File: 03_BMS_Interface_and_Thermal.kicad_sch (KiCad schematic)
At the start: 43 parts, among them J1 HDR-1X17_2.54mm [C22549], J2 S16B-XH-A [C157933]

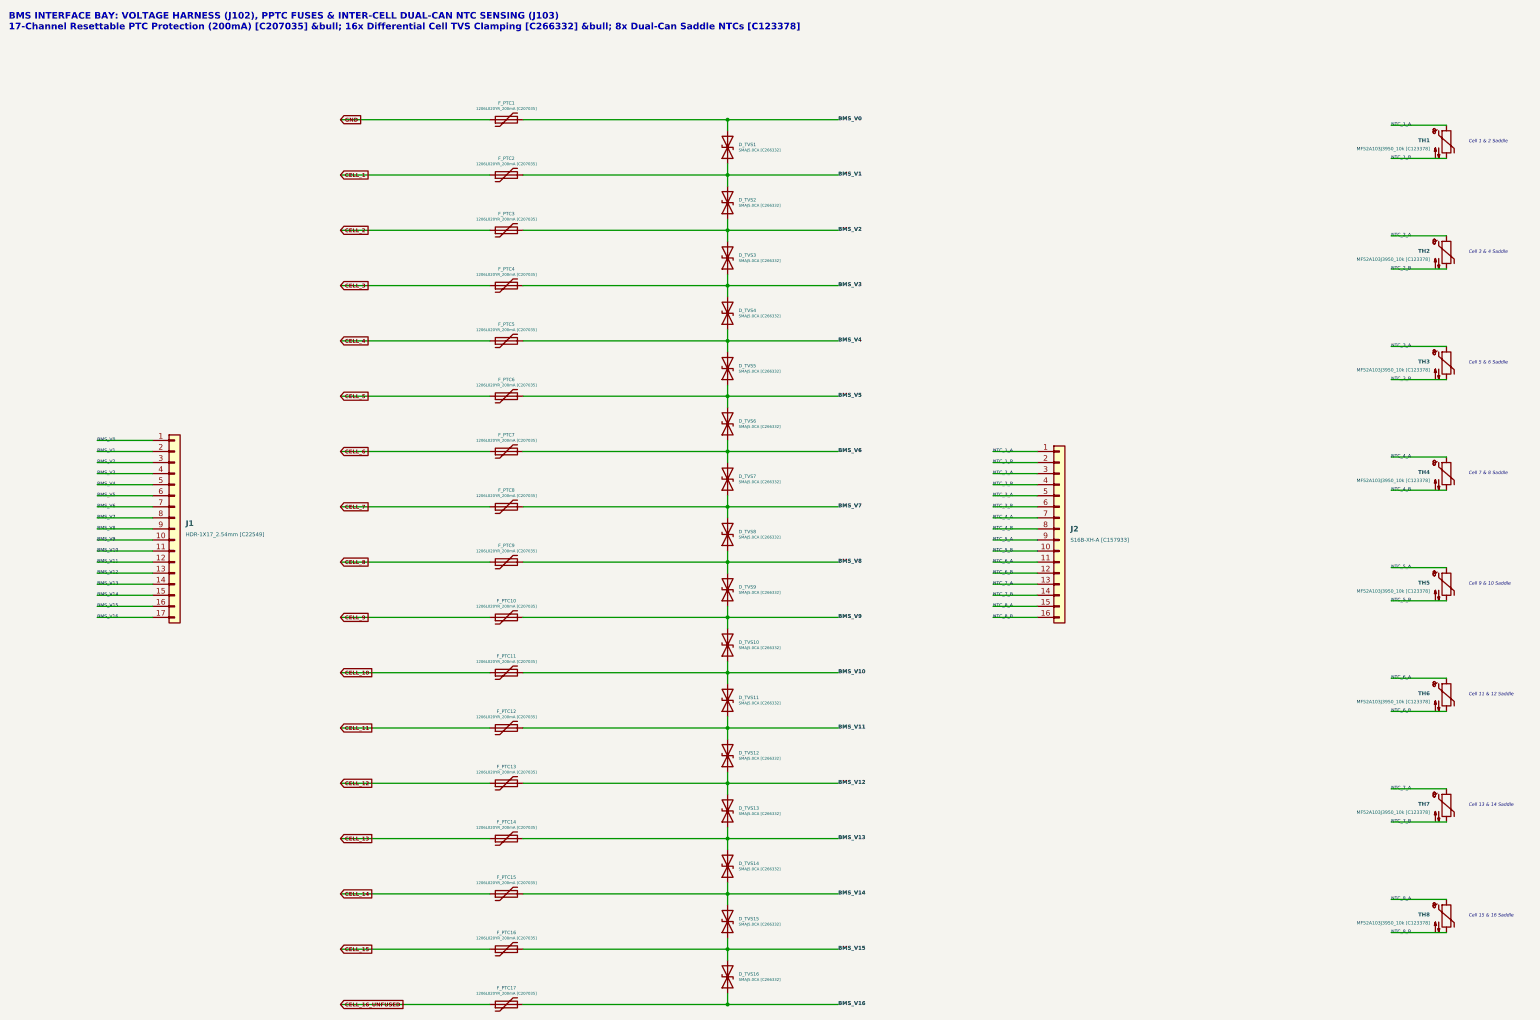
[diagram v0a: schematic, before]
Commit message: Convert pack to 14S with 7 NTC sensors, JST XH harness connectors, all-JLC BOM
- Schematic regenerated: 14 cells, 15-wire BMS sense on JST XH B15B-XH-A,
  7x 10k B3950 NTC saddles on JST XH B14B-XH-A, per-cell test loops and
  reverse-insertion indicator, power path with 5x20 fuse and M4 lugs.
- Fixes: HV zener was reversed, 4.7k/1206 HV LED resistor dissipated 0.68W
  (now 22k), 24V PPTCs on sense taps replaced with 60V MF-MSMF010-2,
  fuse-blown LED polarity corrected.
- Banana jacks (not stocked at LCSC) replaced by Keystone 5000/5001 loops.
- PCB re-laid out on the A4 (297x210) 4-layer outline: 8+6 cell columns,
  zones for cell links, sense routed on In1, NTC pairs on In2.
- ERC 0, DRC 0 (all severities), 0 unconnected, 0 schematic parity issues.
- Added Gerbers/drill zip, JLCPCB BOM + CPL, schematic PDF, renders, and the
  generator scripts in tools/.

Co-Authored-By: Claude Opus 5.5 <noreply@anthropic.com>
Claude-Session: https://claude.ai/code/session_01SDBUxKR8a94h5ECbt5NLbF
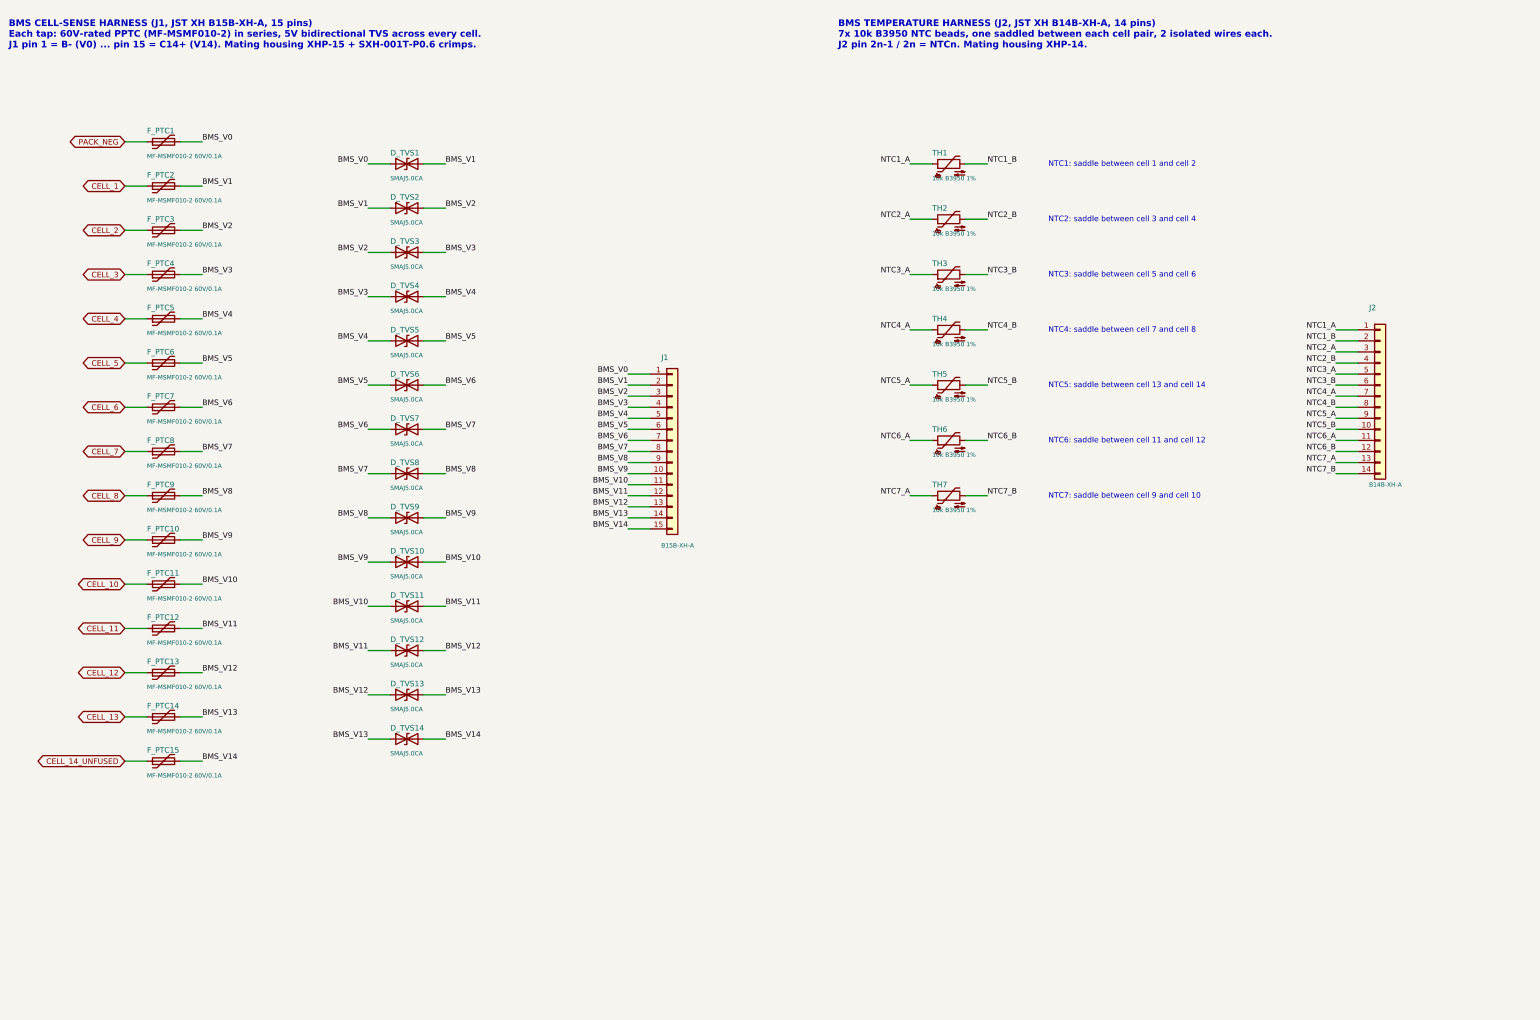
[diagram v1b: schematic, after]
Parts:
- removed D_TVS15, D_TVS16: SMAJ5.0CA [C266332], Diode_SMD:D_SMA, symbol Device:D_TVS
- removed F_PTC16, F_PTC17: 1206L020YR_200mA [C207035], Resistor_SMD:R_1206_3216Metric, symbol Device:Polyfuse
- removed J1: HDR-1X17_2.54mm [C22549], Connector_PinHeader_2.54mm:PinHeader_1x17_P2.54mm_Horizontal, symbol Connector_Generic:Conn_01x17
- removed J2: S16B-XH-A [C157933], Connector_JST:JST_XH_S16B-XH-A_1x16_P2.50mm_Horizontal, symbol Connector_Generic:Conn_01x16
- removed TH8: MF52A103J3950_10k [C123378], Resistor_THT:R_Axial_DIN0204_L3.6mm_D1.6mm_P2.54mm_Vertical, symbol Device:Thermistor_NTC
- added J1: B15B-XH-A, Connector_JST:JST_XH_B15B-XH-A_1x15_P2.50mm_Vertical, symbol Connector_Generic:Conn_01x15
- added J2: B14B-XH-A, Connector_JST:JST_XH_B14B-XH-A_1x14_P2.50mm_Vertical, symbol Connector_Generic:Conn_01x14
- D_TVS1, D_TVS10, D_TVS11, D_TVS12, D_TVS13, D_TVS14, D_TVS2, D_TVS3, D_TVS4, D_TVS5, D_TVS6, D_TVS7, D_TVS8, D_TVS9: value SMAJ5.0CA [C266332] -> SMAJ5.0CA; JLCPCB Part # C266332 -> (none); LCSC C266332 -> C5174731; Manufacturer (none) -> JSCJ
- F_PTC1, F_PTC10, F_PTC11, F_PTC12, F_PTC13, F_PTC14, F_PTC15, F_PTC2, F_PTC3, F_PTC4, F_PTC5, F_PTC6, F_PTC7, F_PTC8, F_PTC9: value 1206L020YR_200mA [C207035] -> MF-MSMF010-2 60V/0.1A; footprint Resistor_SMD:R_1206_3216Metric -> Fuse:Fuse_1812_4532Metric; JLCPCB Part # C207035 -> (none); LCSC C207035 -> C12430; MPN 1206L020YR -> MF-MSMF010-2; Manufacturer (none) -> BOURNS
- TH1, TH2, TH3, TH4, TH5, TH6, TH7: value MF52A103J3950_10k [C123378] -> 10k B3950 1%; JLCPCB Part # C123378 -> (none); LCSC C123378 -> C13879; MPN MF52A103J3950 -> MF52A103F3950; Manufacturer (none) -> Nanjing Shiheng
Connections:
- net BMS_V0: now also D_TVS1.1 (A1), J1.1 (Pin_1); no longer D_TVS1.2 (A2)
- net BMS_V1: now also D_TVS1.2 (A2), D_TVS2.1 (A1), J1.2 (Pin_2); no longer D_TVS1.1 (A1), D_TVS2.2 (A2)
- net BMS_V10: now also D_TVS10.2 (A2), D_TVS11.1 (A1), J1.11 (Pin_11); no longer D_TVS10.1 (A1), D_TVS11.2 (A2)
- net BMS_V11: now also D_TVS11.2 (A2), D_TVS12.1 (A1), J1.12 (Pin_12); no longer D_TVS11.1 (A1), D_TVS12.2 (A2)
- net BMS_V12: now also D_TVS12.2 (A2), D_TVS13.1 (A1), J1.13 (Pin_13); no longer D_TVS12.1 (A1), D_TVS13.2 (A2)
- net BMS_V13: now also D_TVS13.2 (A2), D_TVS14.1 (A1), J1.14 (Pin_14); no longer D_TVS13.1 (A1), D_TVS14.2 (A2)
- net BMS_V14: now also D_TVS14.2 (A2), J1.15 (Pin_15); no longer D_TVS14.1 (A1)
- net BMS_V2: now also D_TVS2.2 (A2), D_TVS3.1 (A1), J1.3 (Pin_3); no longer D_TVS2.1 (A1), D_TVS3.2 (A2)
- net BMS_V3: now also D_TVS3.2 (A2), D_TVS4.1 (A1), J1.4 (Pin_4); no longer D_TVS3.1 (A1), D_TVS4.2 (A2)
- net BMS_V4: now also D_TVS4.2 (A2), D_TVS5.1 (A1), J1.5 (Pin_5); no longer D_TVS4.1 (A1), D_TVS5.2 (A2)
- net BMS_V5: now also D_TVS5.2 (A2), D_TVS6.1 (A1), J1.6 (Pin_6); no longer D_TVS5.1 (A1), D_TVS6.2 (A2)
- net BMS_V6: now also D_TVS6.2 (A2), D_TVS7.1 (A1), J1.7 (Pin_7); no longer D_TVS6.1 (A1), D_TVS7.2 (A2)
- net BMS_V7: now also D_TVS7.2 (A2), D_TVS8.1 (A1), J1.8 (Pin_8); no longer D_TVS7.1 (A1), D_TVS8.2 (A2)
- net BMS_V8: now also D_TVS8.2 (A2), D_TVS9.1 (A1), J1.9 (Pin_9); no longer D_TVS8.1 (A1), D_TVS9.2 (A2)
- net BMS_V9: now also D_TVS10.1 (A1), D_TVS9.2 (A2), J1.10 (Pin_10); no longer D_TVS10.2 (A2), D_TVS9.1 (A1)
- net CELL_14 renamed CELL_14_UNFUSED
- net GND renamed PACK_NEG
- net NTC_1_A renamed NTC1_A
- net NTC1_A: now also J2.1 (Pin_1)
- net NTC_1_B renamed NTC1_B
- net NTC1_B: now also J2.2 (Pin_2)
- net NTC_2_A renamed NTC2_A
- net NTC2_A: now also J2.3 (Pin_3)
- net NTC_2_B renamed NTC2_B
- net NTC2_B: now also J2.4 (Pin_4)
- net NTC_3_A renamed NTC3_A
- net NTC3_A: now also J2.5 (Pin_5)
- net NTC_3_B renamed NTC3_B
- net NTC3_B: now also J2.6 (Pin_6)
- net NTC_4_A renamed NTC4_A
- net NTC4_A: now also J2.7 (Pin_7)
- net NTC_4_B renamed NTC4_B
- net NTC4_B: now also J2.8 (Pin_8)
- net NTC_5_A renamed NTC5_A
- net NTC5_A: now also J2.9 (Pin_9)
- net NTC_5_B renamed NTC5_B
- net NTC5_B: now also J2.10 (Pin_10)
- net NTC_6_A renamed NTC6_A
- net NTC6_A: now also J2.11 (Pin_11)
- net NTC_6_B renamed NTC6_B
- net NTC6_B: now also J2.12 (Pin_12)
- net NTC_7_A renamed NTC7_A
- net NTC7_A: now also J2.13 (Pin_13)
- net NTC_7_B renamed NTC7_B
- net NTC7_B: now also J2.14 (Pin_14)
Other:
- note added: "BMS CELL-SENSE HARNESS (J1, JST XH B15B-XH-A, 15 pins) Each tap: 60V-rated PPTC (MF-MSMF010-2) in series, 5V bidirectional TVS across every cell. J1 pin 1 = B- (V0) ... pin 15 = C14+ (V14). Mating housing XHP-15 + SXH-001T-P0.6 crimps."
- note added: "BMS TEMPERATURE HARNESS (J2, JST XH B14B-XH-A, 14 pins) 7x 10k B3950 NTC beads, one saddled between each cell pair, 2 isolated wires each. J2 pin 2n-1 / 2n = NTCn. Mating housing XHP-14."
- note added: "NTC1: saddle between cell 1 and cell 2"
- note added: "NTC2: saddle between cell 3 and cell 4"
- note added: "NTC3: saddle between cell 5 and cell 6"
- note added: "NTC4: saddle between cell 7 and cell 8"
- note added: "NTC5: saddle between cell 13 and cell 14"
- note added: "NTC6: saddle between cell 11 and cell 12"
- note added: "NTC7: saddle between cell 9 and cell 10"
- note removed: "BMS INTERFACE BAY: VOLTAGE HARNESS (J102), PPTC FUSES & INTER-CELL DUAL-CAN NTC SENSING (J103) 17-Channel Resettable PTC Protection (200mA) [C207035] &bull; 16x Differential Cell TVS Clamping [C266332] &bull; 8x Dual-Can Saddle NTCs [C123378]"
- note removed: "Cell 1 & 2 Saddle"
- note removed: "Cell 11 & 12 Saddle"
- note removed: "Cell 13 & 14 Saddle"
- note removed: "Cell 15 & 16 Saddle"
- note removed: "Cell 3 & 4 Saddle"
- note removed: "Cell 5 & 6 Saddle"
- note removed: "Cell 7 & 8 Saddle"
- note removed: "Cell 9 & 10 Saddle"
- company: Antigravity Battery Engineering -> Battery Pack Breakout - 14S / A4
- title: BMS INTERFACE BAY: VOLTAGE HARNESS, PPTCS & THERMAL MONITORING -> BMS INTERFACE: 15-WIRE CELL SENSE + 7x NTC

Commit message: Mirror the two cell columns (7+7) and move every external connector to the top edge
- Cells 1-7 down the left column, 8-14 up the right, identical row spacing;
  B- now lands at the top-left corner and cell 14+ at the top-right.
- Top edge, left to right: J2 NTC, B- lug, J1 balance (centred), PACK+ lug,
  5x20 fuse. Balance pin 1 = B- on the left, matching the cell order.
- PPTC/TVS sense block sits directly under J1; sense taps fan in on In1,
  NTC pairs run up to J2 on In2. NTCs renumbered along the series path.
- Pack TVS and HV indicator next to PACK+, PACK- return on a B.Cu strip.
- Mid-board M3 holes moved into the channel; wiring guide on silkscreen.
- ERC 0, DRC 0 (all severities), 0 unconnected, 0 parity issues.

Co-Authored-By: Claude Opus 5.5 <noreply@anthropic.com>
Claude-Session: https://claude.ai/code/session_01SDBUxKR8a94h5ECbt5NLbF
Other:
- note added: "NTC4: saddle between cell 6 and cell 7"
- note added: "NTC5: saddle between cell 9 and cell 10"
- note added: "NTC7: saddle between cell 13 and cell 14"
- note removed: "NTC4: saddle between cell 7 and cell 8"
- note removed: "NTC5: saddle between cell 13 and cell 14"
- note removed: "NTC7: saddle between cell 9 and cell 10"
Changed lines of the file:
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@@
 		)
 	)
-	(text "NTC4: saddle between cell 7 and cell 8"
+	(text "NTC4: saddle between cell 6 and cell 7"
 		(exclude_from_sim no)
 		(at 264.16 93.345 0)
@@
 		)
 	)
-	(text "NTC5: saddle between cell 13 and cell 14"
+	(text "NTC5: saddle between cell 9 and cell 10"
 		(exclude_from_sim no)
 		(at 264.16 106.045 0)
@@
 		)
 	)
-	(text "NTC7: saddle between cell 9 and cell 10"
+	(text "NTC7: saddle between cell 13 and cell 14"
 		(exclude_from_sim no)
 		(at 264.16 131.445 0)

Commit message: Senior-level layout rework: equal-resistance cell links, uniform pitch, sense spine
- Uniform 27.6 mm cell pitch (4.8 mm air gap around every cell).
- All 13 cell-to-cell links are identical copper straps (F.Cu + B.Cu); the
  cell 7->8 strap across the channel is widened to 16.15 mm so its
  resistance matches. 2-D field solve: 0.260 mOhm per link, 0.08 % spread
  (tools/acir.py, docs/acir_check.txt).
- Centre channel is now a sense spine: a 60 V PPTC at every node and one
  In1 bus into J1; per-cell TVS moved to SOD-323 (LKS05D3-B) directly under
  J1 so the whole BMS protection block sits on the top edge.
- Outer margins: per-cell test loops, reverse-cell LED, writable V/IR box.
- Top edge: B- lug, HV indicator + pack TVS, J1, J2, PACK+ lug, fuse.
- Shared geometry module (tools/geom.py) used by layout and ACIR check.
- ERC 0, DRC 0, 0 unconnected, 0 parity issues.

Co-Authored-By: Claude Opus 5.5 <noreply@anthropic.com>
Claude-Session: https://claude.ai/code/session_01SDBUxKR8a94h5ECbt5NLbF
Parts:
- D_TVS1, D_TVS10, D_TVS11, D_TVS12, D_TVS13, D_TVS14, D_TVS2, D_TVS3, D_TVS4, D_TVS5, D_TVS6, D_TVS7, D_TVS8, D_TVS9: value SMAJ5.0CA -> LKS05D3-B; footprint Diode_SMD:D_SMA -> Diode_SMD:D_SOD-323; LCSC C5174731 -> C2984829; MPN SMAJ5.0CA -> LKS05D3-B; Manufacturer JSCJ -> LANKE
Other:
- note added: "BMS CELL-SENSE HARNESS (J1, JST XH B15B-XH-A, 15 pins) Each tap: 60V PPTC (MF-MSMF010-2) next to its cell node, 5V bidir TVS (LKS05D3-B) across every cell at J1. J1 pin 1 = B- (V0) ... pin 15 = C14+ (V14). Mating housing XHP-15 + SXH-001T-P0.6 crimps."
- note added: "NTC5: saddle between cell 13 and cell 14"
- note added: "NTC7: saddle between cell 9 and cell 10"
- note removed: "BMS CELL-SENSE HARNESS (J1, JST XH B15B-XH-A, 15 pins) Each tap: 60V-rated PPTC (MF-MSMF010-2) in series, 5V bidirectional TVS across every cell. J1 pin 1 = B- (V0) ... pin 15 = C14+ (V14). Mating housing XHP-15 + SXH-001T-P0.6 crimps."
- note removed: "NTC5: saddle between cell 9 and cell 10"
- note removed: "NTC7: saddle between cell 13 and cell 14"

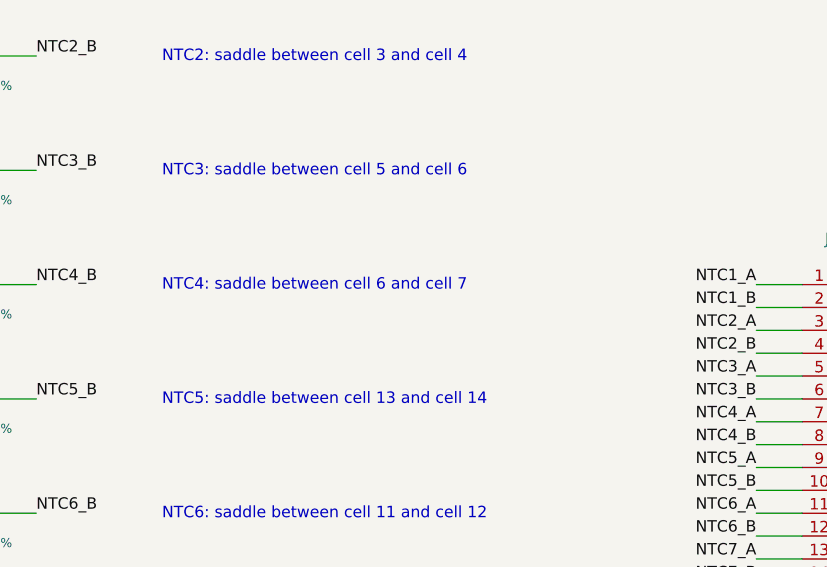
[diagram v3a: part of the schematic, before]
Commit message: Make the board mirror-symmetric about its centre line
- NTCs: 3 per side in mirrored gaps, NTC4 on the centre line at the
  cell 7->8 bus (J2 pins 7/8); J2 pin 2n-1/2n = NTCn kept.
- Sense spine exactly symmetric: tap-7 PPTC and its bus line on the centre
  line, side buses mirrored, J1 fan symmetric.
- Per-cell LED strings: series order chosen per cell so mirrored twins use
  the same parts in the same places (function unchanged).
- TVS chain under J1 mirrored; the centre pair stands vertically either side
  of lane 7.
- HV indicator + pack TVS centred at J2's mirror position; top-band copper
  mirrored; 4 corner fiducials.
- tools/symcheck.py audits mirror partners: only J2, the HV block and the
  single PACK+ fuse (+ its LED) are one-of-a-kind.
- ERC 0, DRC 0, 0 unconnected, 0 parity; ACIR spread 0.08 %.

Co-Authored-By: Claude Opus 5.5 <noreply@anthropic.com>
Claude-Session: https://claude.ai/code/session_01SDBUxKR8a94h5ECbt5NLbF
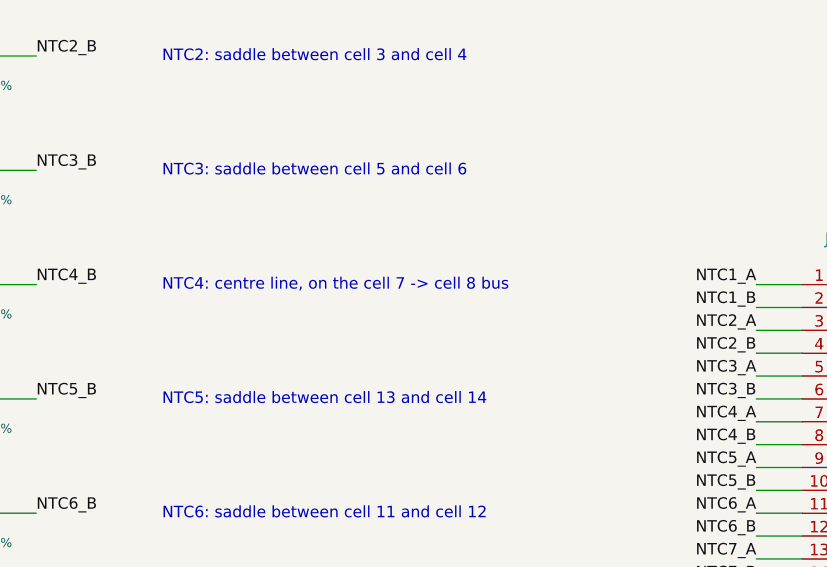
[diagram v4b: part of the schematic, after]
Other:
- note added: "NTC4: centre line, on the cell 7 -> cell 8 bus"
- note removed: "NTC4: saddle between cell 6 and cell 7"
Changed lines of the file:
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@@
 		)
 	)
-	(text "NTC4: saddle between cell 6 and cell 7"
+	(text "NTC4: centre line, on the cell 7 -> cell 8 bus"
 		(exclude_from_sim no)
 		(at 264.16 93.345 0)
